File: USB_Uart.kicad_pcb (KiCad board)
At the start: 2 copper layers, 15 parts, among them J1 USB_B, J2 Conn_01x10, J3 Conn_01x04, J4 Conn_01x04, U1 CP2104, U2 TPD4EUSB30

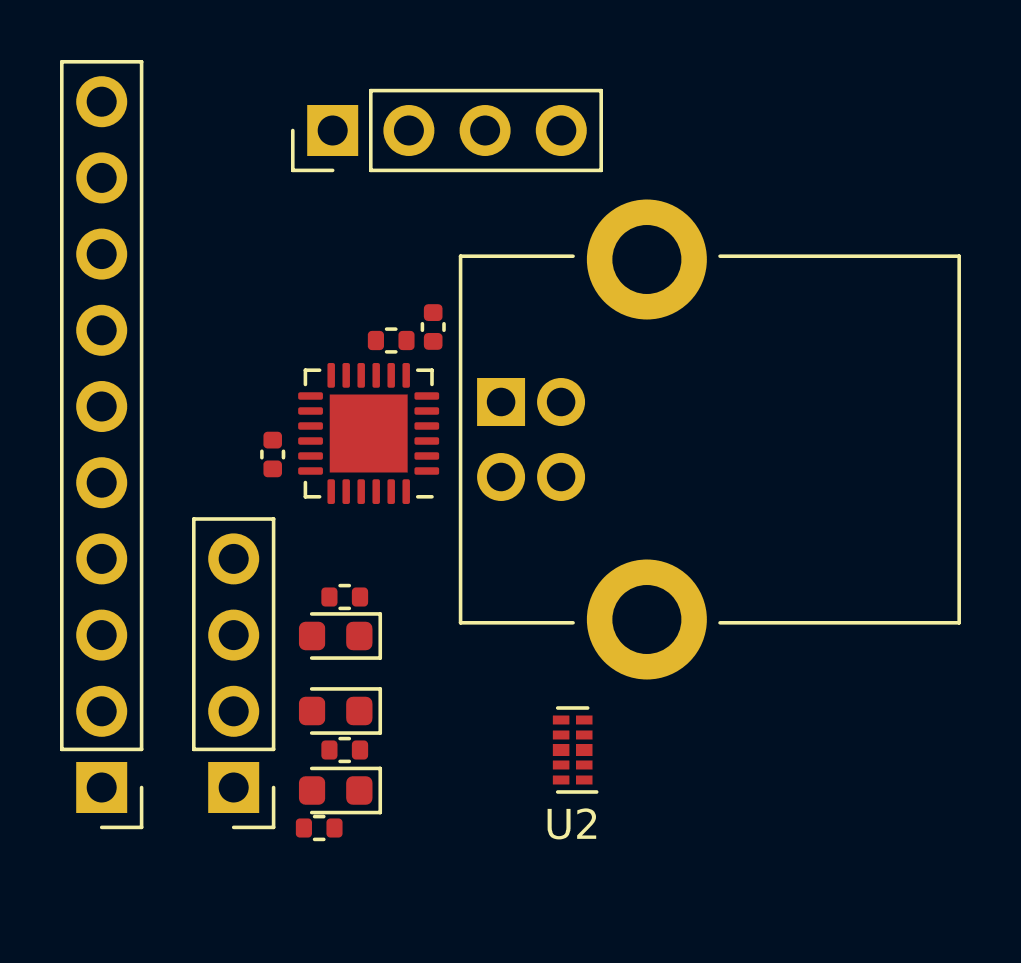
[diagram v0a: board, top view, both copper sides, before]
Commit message: Layout footprints,  Adjust schematic
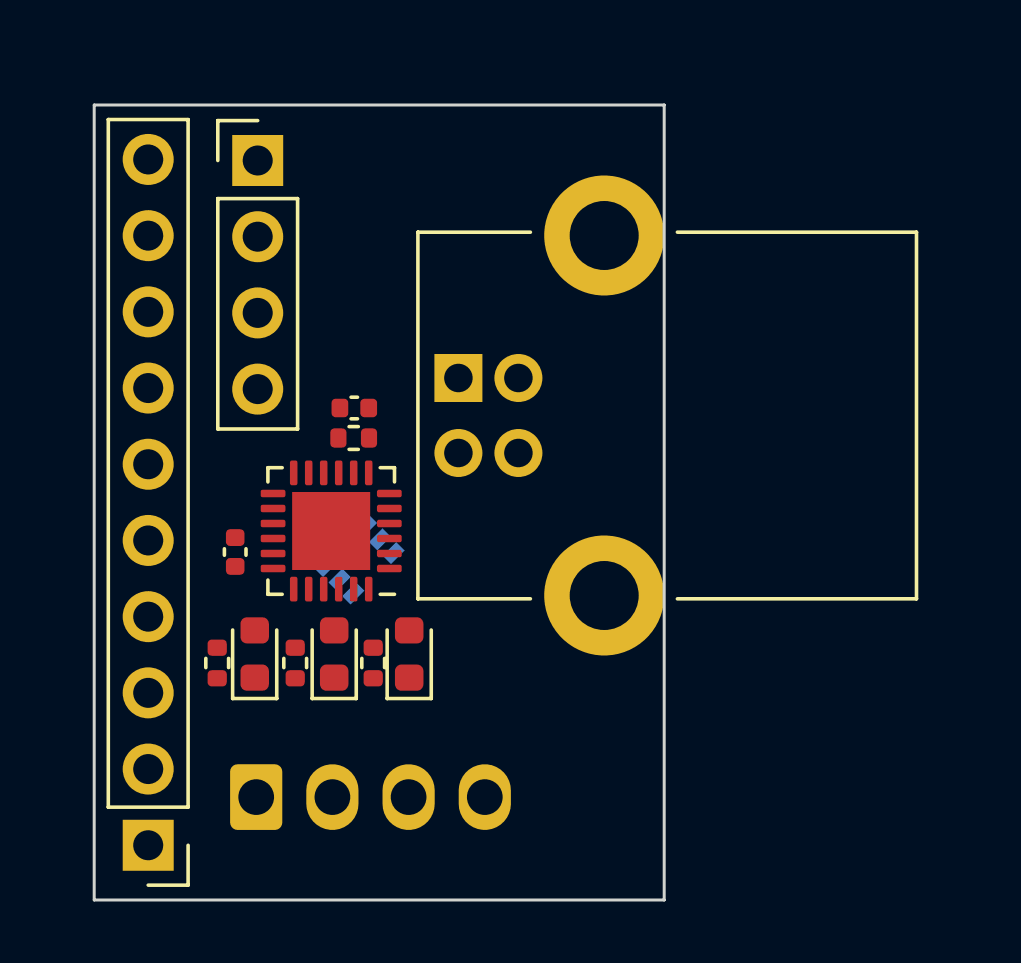
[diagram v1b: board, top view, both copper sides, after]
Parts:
- J3: footprint Connector_PinHeader_2.54mm:PinHeader_1x04_P2.54mm_Vertical -> Connector_Molex:Molex_KK-254_AE-6410-04A_1x04_P2.54mm_Vertical; moved to B.Cu
- U2: footprint Package_SON:USON-10_2.5x1.0mm_P0.5mm -> Package_TO_SOT_SMD:SOT-363_SC-70-6; moved to B.Cu
- moved U2 9.53 mm to (68.7, 70.2), turned to -135 degrees
- moved R2 6.47 mm to (63.9, 73.6), turned to -90 degrees
- moved D3 5.29 mm to (65.2, 73.3), turned to 90 degrees
- moved C1 3.77 mm to (68.5, 65.1), turned to 180 degrees
- moved C3 3.48 mm to (64.5, 69.9)
- moved U1 3.48 mm to (67.7, 69.2)
- moved R1 3.48 mm to (68.5, 66.1)
- moved R3 3.34 mm to (66.5, 73.6), turned to 90 degrees
- moved J4 2.69 mm to (65.2, 56.9), turned to 0 degrees
- moved D2 2.52 mm to (70.3, 73.3), turned to 90 degrees
- moved J2 2.47 mm to (61.6, 79.7)
- moved R4 2.40 mm to (69.1, 73.6), turned to 90 degrees
- moved D1 1.90 mm to (67.8, 73.3), turned to 90 degrees
- moved J1 1.63 mm to (71.9, 64.1)
- moved J3 0.82 mm to (65.2, 78.1), turned to 0 degrees
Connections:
- D1 pad 2: Tx -> Rx
- D2 pad 2: Rx -> Tx
- J3 pad 2: Tx -> Rx
- J3 pad 3: Rx -> Tx
- U2 pad 1: D+ -> D-
- U2 pad 2: D- -> GND
- U2 pad 3: GND -> D+
- U2 pad 5: Rx -> (no net)
- U2 pad 6: unconnected-(U2-Pad6) -> Rx
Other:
- board outline added: 19 x 26.5 mm

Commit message: Switch to USB-B-Micro, add routing
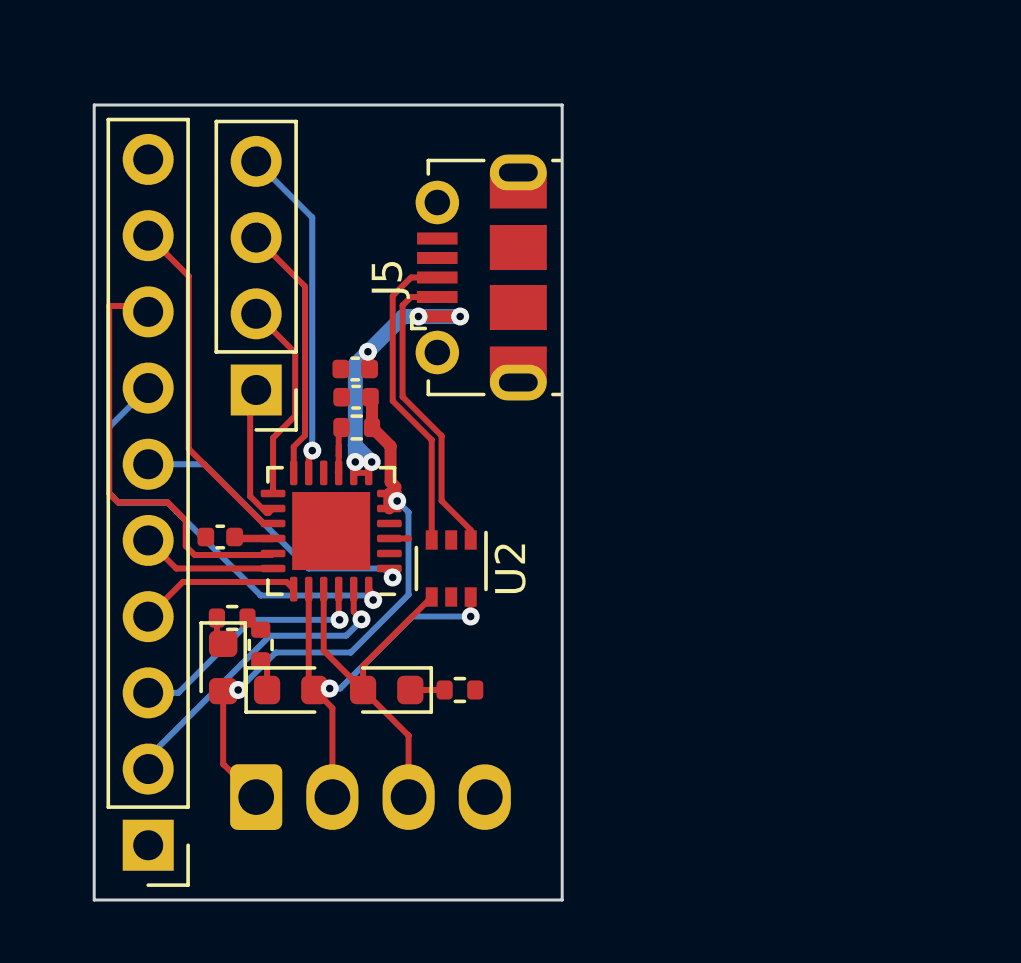
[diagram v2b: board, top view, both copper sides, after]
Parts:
- removed J1: USB_B, Connector_USB:USB_B_Lumberg_2411_02_Horizontal
- added C2: 4.7uf, Capacitor_SMD:C_0402_1005Metric, F.Cu at (68.5, 63.8)
- added J5: USB_B_Mini, Connector_USB:USB_Micro-B_Molex-105017-0001, F.Cu at (72.7, 60.8)
- U2: moved to F.Cu
- moved J4 7.65 mm to (65.2, 64.5), turned to 180 degrees
- moved U2 3.06 mm to (71.7, 70.5), turned to -90 degrees
- moved R4 3.03 mm to (72.0, 74.5), turned to 0 degrees
- moved D1 1.88 mm to (66.3, 74.5), turned to 0 degrees
- moved R2 1.58 mm to (64.4, 72.1), turned to 0 degrees
- moved D2 1.42 mm to (69.5, 74.5), turned to 180 degrees
- moved R3 1.30 mm to (65.3, 73.0)
- moved D3 1.14 mm to (64.1, 73.8), turned to -90 degrees
- moved C3 0.71 mm to (64.0, 69.4), turned to 180 degrees
- moved C1 0.36 mm to (68.5, 64.7)
- moved R1 0.36 mm to (68.5, 65.8)
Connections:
- net Vcc renamed VDD
- D3 pad 1: GND -> Net-(D3-Pad1)
- D3 pad 2: Net-(D3-Pad2) -> Vdd
- R2 pad 1: Vdd -> Net-(D3-Pad1)
- R2 pad 2: Net-(D3-Pad2) -> GND
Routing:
- net Vdd: track 0.00 -> 19.3 mm, vias 0 -> 2
- net DCD: track 0.00 -> 14.9 mm, vias 0 -> 1
- net SUSP: track 0.00 -> 14.5 mm
- net Rx: track 0.00 -> 14.1 mm, vias 0 -> 2
- net Tx: track 0.00 -> 12.2 mm
- net _SUSP: track 0.00 -> 11.5 mm
- net GP3: track 0.00 -> 11.2 mm, vias 0 -> 1
- net D+: track 0.00 -> 11.1 mm
- net DTR: track 0.00 -> 10.5 mm, vias 0 -> 1
- net VBUS: track 0.00 -> 10.1 mm, vias 0 -> 5
- net RI: track 0.00 -> 10.1 mm, vias 0 -> 1
- net D-: track 0.00 -> 10.0 mm
- net GP2: track 0.00 -> 8.67 mm
- net DSR: track 0.00 -> 8.42 mm, vias 0 -> 1
- net GP1: track 0.00 -> 6.83 mm
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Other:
- board size 19 x 26.5 mm -> 15.6 x 26.5 mm

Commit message: Add files via upload
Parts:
- moved C3 0.87 mm to (64.2, 68.5), turned to 90 degrees
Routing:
- net SUSP: track 14.5 -> 11.0 mm
- net D-: track 10.0 -> 12.5 mm, vias 0 -> 2
- net DCD: track 14.9 -> 12.8 mm, vias 1 -> 2
- net D+: track 11.1 -> 12.0 mm
- net Vdd: track 19.3 -> 19.8 mm
- net GND: track 0.00 -> 0.36 mm, vias 0 -> 1

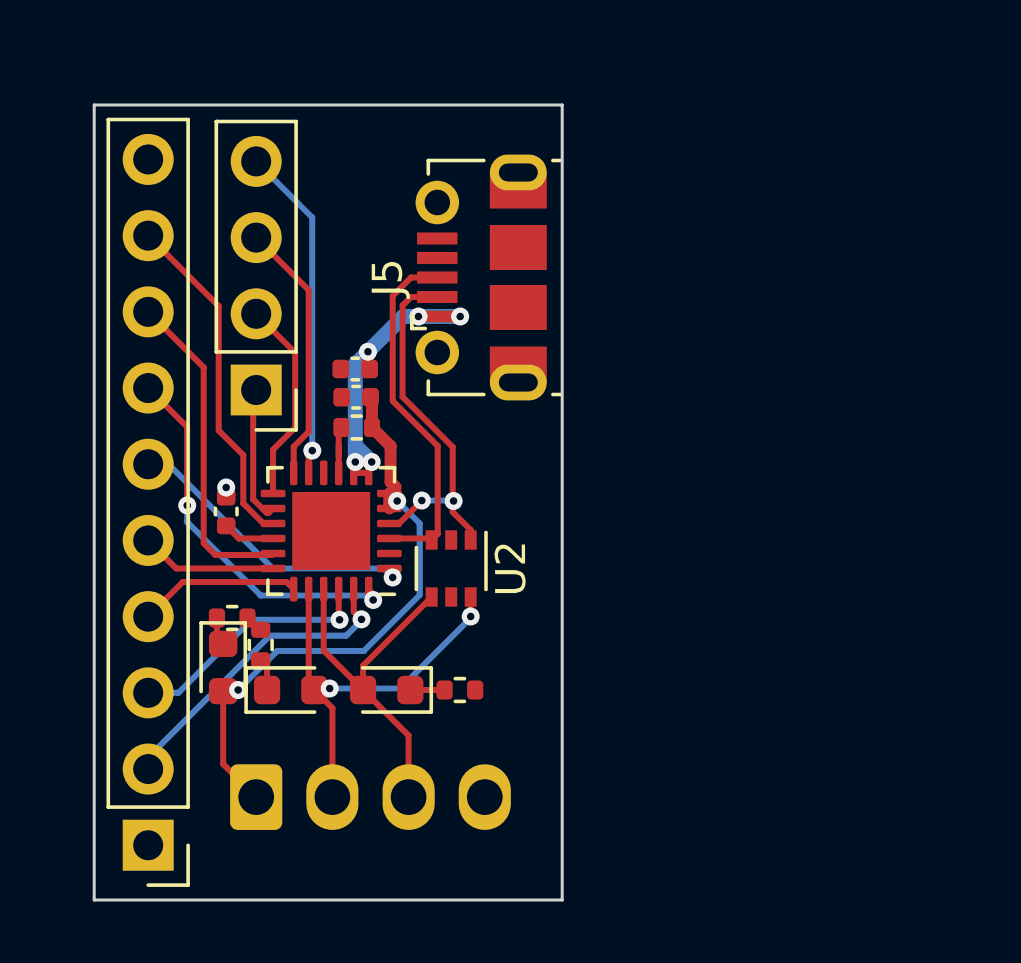
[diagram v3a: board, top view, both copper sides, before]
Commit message: Fix Layout, fill zones.
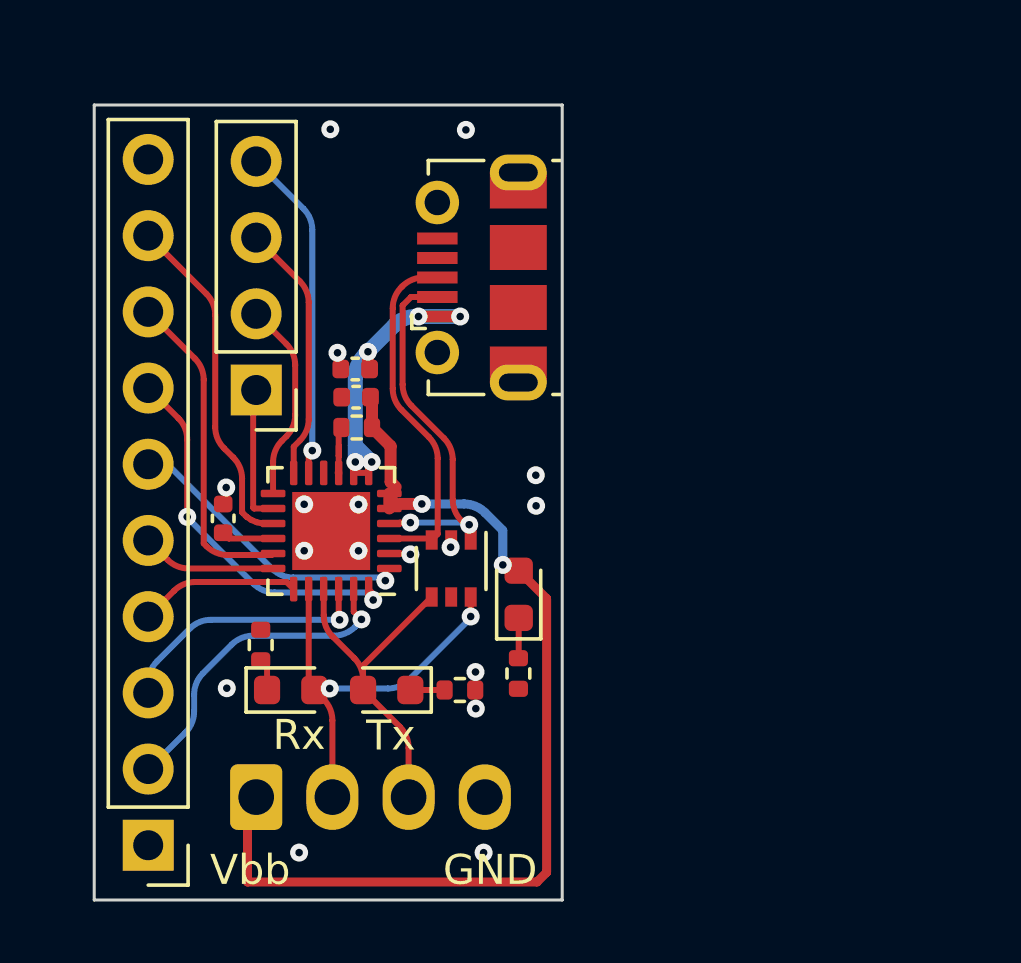
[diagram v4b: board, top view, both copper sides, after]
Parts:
- moved D3 10.1 mm to (74.0, 71.3), turned to 90 degrees
- moved R2 9.72 mm to (73.9, 74.0), turned to -90 degrees
- moved C3 0.25 mm to (64.1, 68.8)
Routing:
- net Vdd: track 19.8 -> 33.6 mm
- net GND: track 0.36 -> 1.35 mm, vias 1 -> 17
- added copper zone on B.Cu, net GND
- added copper zone on F.Cu, net GND
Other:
- board text added: "GND"
- board text added: "Rx"
- board text added: "Tx"
- board text added: "Vbb"

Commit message: Fine tuning traces and fills.  Added Silkscreen
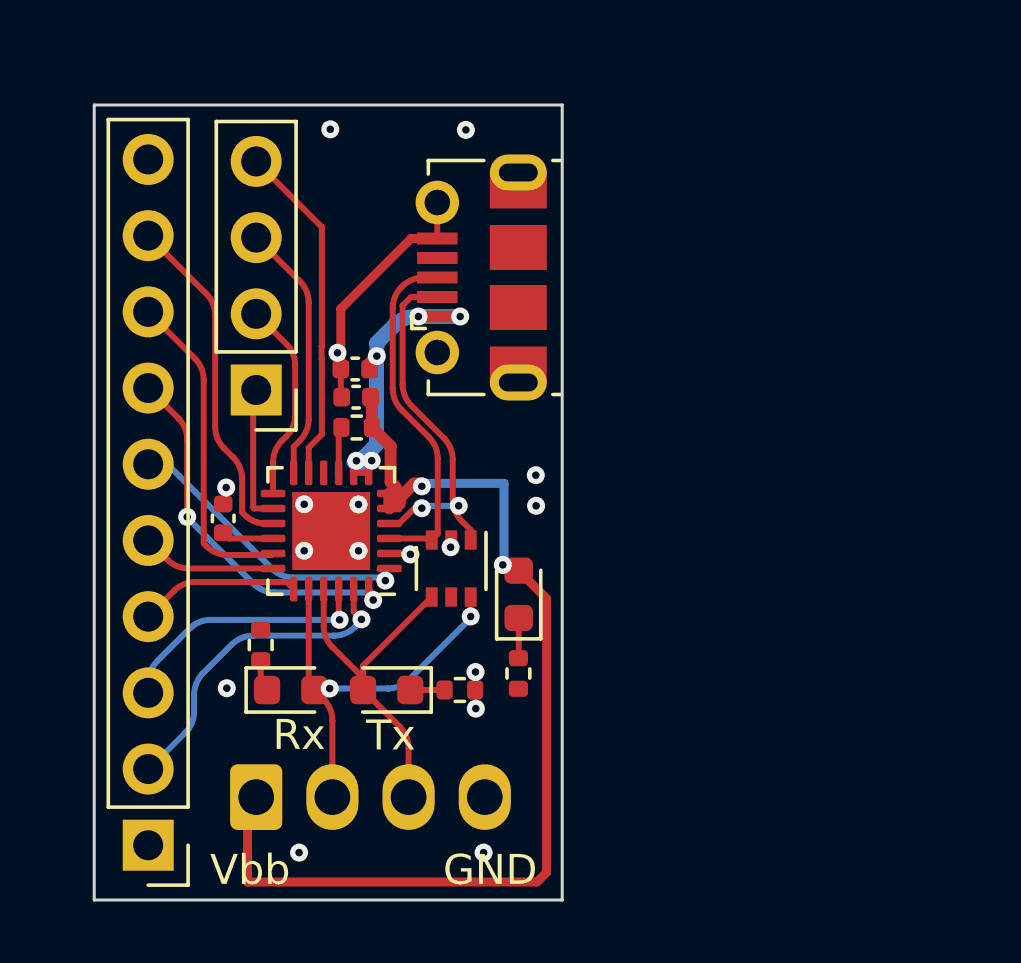
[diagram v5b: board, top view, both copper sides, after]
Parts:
- added REF**: OSHW-Logo2_7.3x6mm_SilkScreen, Symbol:OSHW-Logo2_7.3x6mm_SilkScreen, B.Cu at (71.3, 70.5)
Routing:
- net GND: track 1.35 -> 9.81 mm
- net Vdd: track 33.6 -> 35.4 mm
- net VBUS: track 9.98 -> 10.8 mm
- net GP3: track 11.2 -> 11.5 mm, vias 1 -> 0
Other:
- board text added: "https://github.com/Ccecil/jaUART"

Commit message: First round DRC
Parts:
- moved R3 0.11 mm to (65.3, 72.9)

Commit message: Update files, add BOM and JPG
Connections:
- J2 pad 1: VDD -> Vdd
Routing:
- net Vdd: track 35.4 -> 39.3 mm
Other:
- board size 15.6 x 26.5 mm -> 15.7 x 26.5 mm
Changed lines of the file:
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@@
   (net 24 "Net-(D2-Pad1)")
   (net 25 "Net-(D3-Pad1)")
-  (net 26 "VDD")
-  (net 27 "RST")
-  (net 28 "unconnected-(J5-Pad4)")
+  (net 26 "RST")
+  (net 27 "unconnected-(J5-Pad4)")
   (footprint "LED_SMD:LED_0603_1608Metric" (layer "F.Cu")
     (at 66.35 74.5)
@@
       (net 3 "D+") (pinfunction "D+") (pintype "bidirectional"))
     (pad "4" smd rect locked (at 0.65 -1.4625 90) (size 0.4 1.35) (layers "F.Cu" "F.Paste" "F.Mask")
-      (net 28 "unconnected-(J5-Pad4)") (pinfunction "ID") (pintype "passive"))
+      (net 27 "unconnected-(J5-Pad4)") (pinfunction "ID") (pintype "passive"))
     (pad "5" smd rect locked (at 1.3 -1.4625 90) (size 0.4 1.35) (layers "F.Cu" "F.Paste" "F.Mask")
       (net 4 "GND") (pinfunction "GND") (pintype "power_out"))
@@
     (fp_line (start -1.27 -0.635) (end -0.635 -1.27) (layer "F.Fab") (width 0.1))
     (pad "1" thru_hole rect locked (at 0 0 180) (size 1.7 1.7) (drill 1) (layers *.Cu *.Mask)
-      (net 26 "VDD") (pinfunction "Pin_1") (pintype "passive"))
+      (net 6 "Vdd") (pinfunction "Pin_1") (pintype "passive"))
     (pad "2" thru_hole oval locked (at 0 2.54 180) (size 1.7 1.7) (drill 1) (layers *.Cu *.Mask)
       (net 21 "DTR") (pinfunction "Pin_2") (pintype "passive"))
@@
       (net 13 "_SUSP") (pinfunction "Pin_9") (pintype "passive"))
     (pad "10" thru_hole oval locked (at 0 22.86 180) (size 1.7 1.7) (drill 1) (layers *.Cu *.Mask)
-      (net 27 "RST") (pinfunction "Pin_10") (pintype "passive"))
+      (net 26 "RST") (pinfunction "Pin_10") (pintype "passive"))
     (model "${KICAD6_3DMODEL_DIR}/Connector_PinHeader_2.54mm.3dshapes/PinHeader_1x10_P2.54mm_Vertical.wrl"
       (offset (xyz 0 0 0))
@@
     )
   )
-  (gr_rect (start 59.8 55) (end 75.4 81.5) (layer "Edge.Cuts") (width 0.1) (fill none))
+  (gr_rect (start 59.775 55) (end 75.45 81.55) (layer "Edge.Cuts") (width 0.1) (fill none))
   (gr_text "https://github.com/Ccecil/jaUART" (at 67.17 67.89 270) (layer "B.SilkS")
     (effects (font (size 0.5 0.5) (thickness 0.125)) (justify mirror))
@@
   (segment (start 69.679511 67.567011) (end 69.679511 66.369511) (width 0.4) (layer "F.Cu") (net 6))
   (segment (start 69.679511 66.369511) (end 69.06 65.75) (width 0.4) (layer "F.Cu") (net 6))
+  (segment (start 63.8 80.9) (end 64.91 80.9) (width 0.3) (layer "F.Cu") (net 6))
   (segment (start 69.85 67.7375) (end 69.679511 67.567011) (width 0.4) (layer "F.Cu") (net 6))
   (segment (start 70.7205 67.710497) (end 70.630492 67.620489) (width 0.4) (layer "F.Cu") (net 6))
@@
   (segment (start 73.95 70.5225) (end 74.88 71.4525) (width 0.3) (layer "F.Cu") (net 6))
   (segment (start 69.06 65.75) (end 69.06 64.79) (width 0.4) (layer "F.Cu") (net 6))
+  (segment (start 62.475 79.675) (end 63.75 80.95) (width 0.3) (layer "F.Cu") (net 6))
   (segment (start 69.06 64.79) (end 69.01 64.74) (width 0.4) (layer "F.Cu") (net 6))
+  (segment (start 63.75 80.95) (end 63.8 80.9) (width 0.2) (layer "F.Cu") (net 6))
   (segment (start 74.88 80.58) (end 74.56 80.9) (width 0.3) (layer "F.Cu") (net 6))
+  (segment (start 61.6 79.675) (end 62.475 79.675) (width 0.3) (layer "F.Cu") (net 6))
   (via (at 70.7205 67.710497) (size 0.6) (drill 0.25) (layers "F.Cu" "B.Cu") (net 6))
   (via (at 73.42 70.33) (size 0.6) (drill 0.25) (layers "F.Cu" "B.Cu") (net 6))
@@
   (segment (start 70.820997 67.61) (end 73.46 67.61) (width 0.3) (layer "B.Cu") (net 6))
   (segment (start 70.7205 67.710497) (end 70.820997 67.61) (width 0.3) (layer "B.Cu") (net 6))
-  (segment (start 67.94 67.2525) (end 67.95 67.2625) (width 0.25) (layer "F.Cu") (net 7))
   (segment (start 67.95 65.84) (end 67.95 67.2625) (width 0.2) (layer "F.Cu") (net 7))
   (segment (start 68.04 65.75) (end 67.95 65.84) (width 0.2) (layer "F.Cu") (net 7))
